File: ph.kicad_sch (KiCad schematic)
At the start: 38 parts, among them IC2 ADM3260ARSZ-RL7, J4 pH, U10 REF3020, U11 TPS60400DBV, U12 ADS1115IDGS, U14 TLV271, U15 TLV271

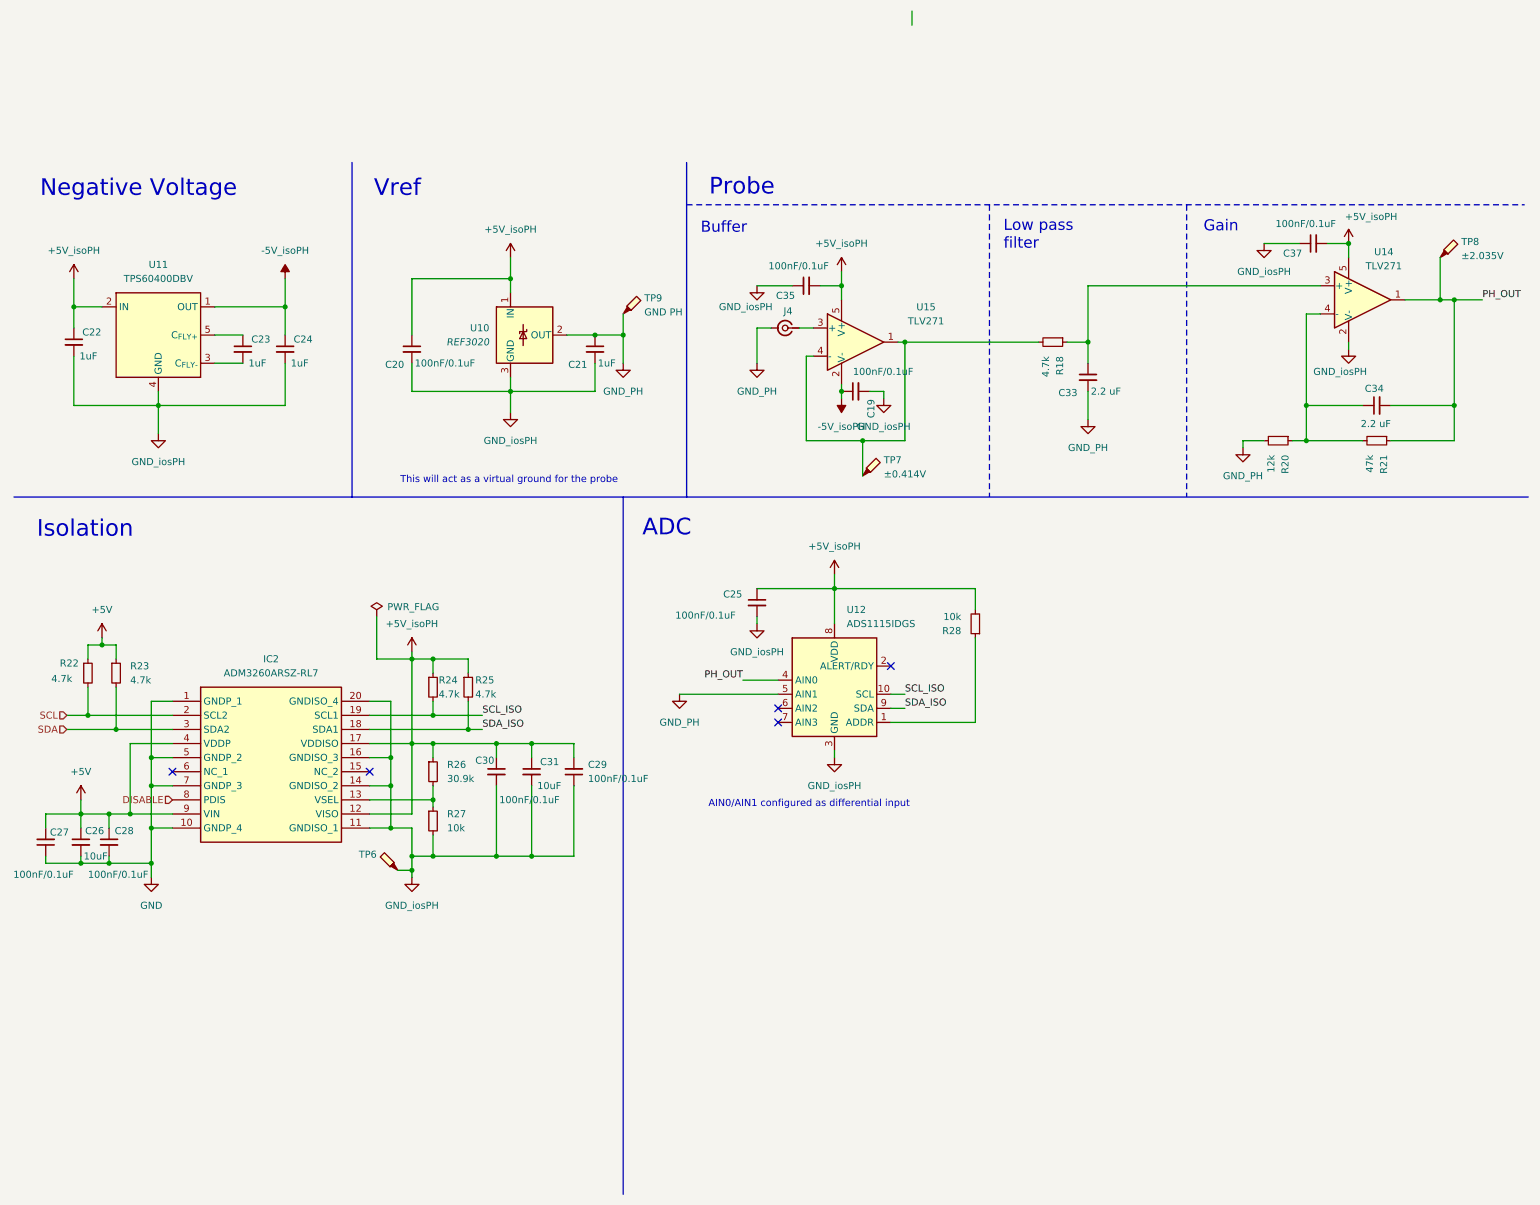
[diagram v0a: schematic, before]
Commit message: Fix ERC warnings
See #28
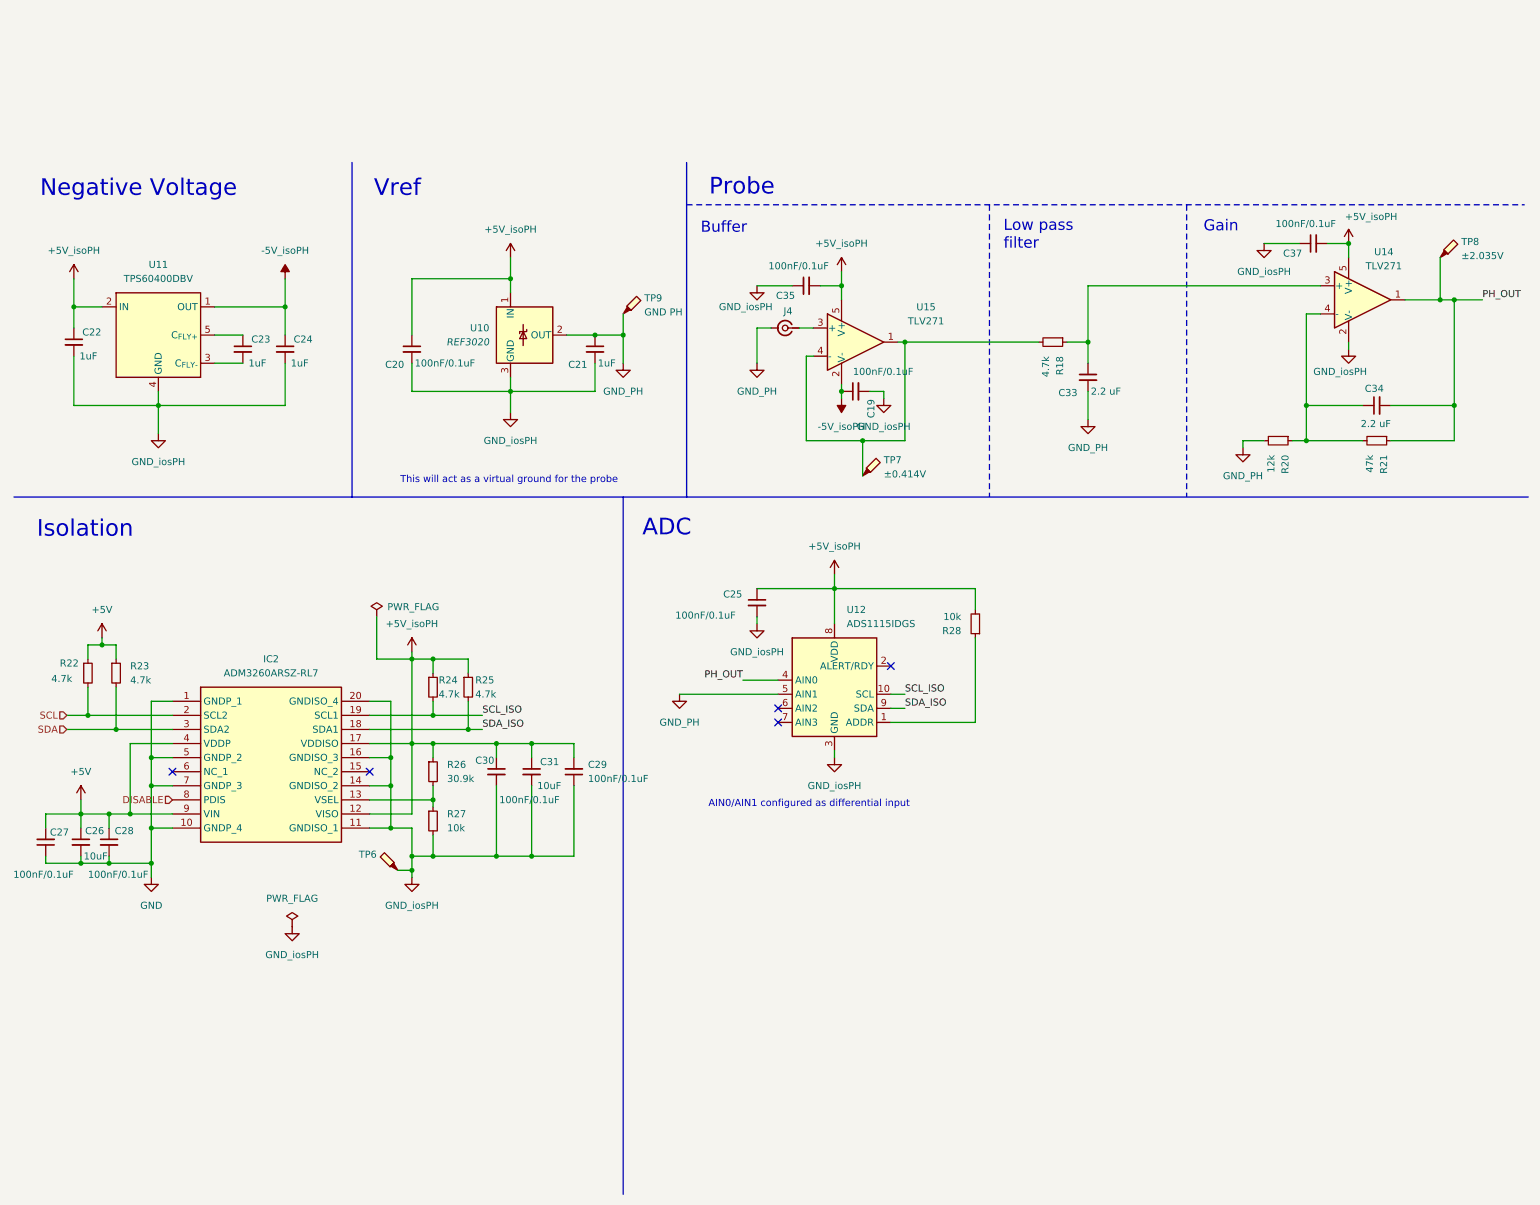
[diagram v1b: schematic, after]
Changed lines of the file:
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@@
 	(wire
 		(pts
-			(xy 173.99 -12.7) (xy 173.99 -15.24)
-		)
-		(stroke
-			(width 0)
-			(type default)
-		)
-	)
-	(wire
-		(pts
 			(xy 157.48 34.29) (xy 161.29 34.29)
 		)
@@
 	)
 	(symbol
+		(lib_id "power:GNDA")
+		(at 62.23 149.86 0)
+		(unit 1)
+		(exclude_from_sim no)
+		(in_bom yes)
+		(on_board yes)
+		(dnp no)
+		(fields_autoplaced yes)
+		(property "Reference" "#PWR0115"
+			(at 62.23 156.21 0)
+			(effects
+				(font
+					(size 1.27 1.27)
+				)
+				(hide yes)
+			)
+		)
+		(property "Value" "GND_iosPH"
+			(at 62.23 154.94 0)
+			(effects
+				(font
+					(size 1.27 1.27)
+				)
+			)
+		)
+		(property "Footprint" ""
+			(at 62.23 149.86 0)
+			(effects
+				(font
+					(size 1.27 1.27)
+				)
+				(hide yes)
+			)
+		)
+		(property "Datasheet" ""
+			(at 62.23 149.86 0)
+			(effects
+				(font
+					(size 1.27 1.27)
+				)
+				(hide yes)
+			)
+		)
+		(property "Description" "Power symbol creates a global label with name \"GNDA\" , analog ground"
+			(at 62.23 149.86 0)
+			(effects
+				(font
+					(size 1.27 1.27)
+				)
+				(hide yes)
+			)
+		)
+		(pin "1"
+		)
+		(instances
+			(project "HydroponicFlowerControl"
+				(path "/b3c8a28b-9ce1-4002-b8e8-ef8cb73fe031/98c7b1ae-5b10-4cce-8f75-2d85473487c0"
+					(reference "#PWR0115")
+					(unit 1)
+				)
+			)
+		)
+	)
+	(symbol
 		(lib_id "Connector:Conn_Coaxial_Small")
 		(at 151.13 41.91 180)
@@
 					(unit 1)
 				)
+			)
+		)
+	)
+	(symbol
+		(lib_id "power:PWR_FLAG")
+		(at 62.23 149.86 0)
+		(unit 1)
+		(exclude_from_sim no)
+		(in_bom yes)
+		(on_board yes)
+		(dnp no)
+		(fields_autoplaced yes)
+		(property "Reference" "#FLG08"
+			(at 62.23 147.955 0)
+			(effects
+				(font
+					(size 1.27 1.27)
+				)
+				(hide yes)
+			)
+		)
+		(property "Value" "PWR_FLAG"
+			(at 62.23 144.78 0)
+			(effects
+				(font
+					(size 1.27 1.27)
+				)
+			)
+		)
+		(property "Footprint" ""
+			(at 62.23 149.86 0)
+			(effects
+				(font
+					(size 1.27 1.27)
+				)
+				(hide yes)
+			)
+		)
+		(property "Datasheet" "~"
+			(at 62.23 149.86 0)
+			(effects
+				(font
+					(size 1.27 1.27)
+				)
+				(hide yes)
+			)
+		)
+		(property "Description" "Special symbol for telling ERC where power comes from"
+			(at 62.23 149.86 0)
+			(effects
+				(font
+					(size 1.27 1.27)
+				)
+				(hide yes)
+			)
+		)
+		(pin "1"
+		)
+		(instances
+			(project "HydroponicFlowerControl"
+				(path "/b3c8a28b-9ce1-4002-b8e8-ef8cb73fe031/98c7b1ae-5b10-4cce-8f75-2d85473487c0"
+					(reference "#FLG08")
+					(unit 1)
+				)

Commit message: Remove TPS60400 (U11) from pH block
Closes #30
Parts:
- removed C19: 100nF/0.1uF, Capacitor_SMD:C_0603_1608Metric, symbol Device:C_Small
- removed C22, C23, C24: 1uF, Capacitor_SMD:C_0603_1608Metric, symbol Device:C_Small
- removed U11: TPS60400DBV, Package_TO_SOT_SMD:SOT-23-5, symbol Regulator_SwitchedCapacitor:TPS60400DBV
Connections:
- net -5V_isoPH is gone; now on net GND_iosPH: U15.2 (V-)
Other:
- note removed: "Negative Voltage"

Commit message: Update pH connector to combined BNC and SMA footprint
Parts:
- J4: footprint Connector_Coaxial:BNC_Amphenol_B6252HB-NPP3G-50_Horizontal -> HydroponicFlowerControl:BNC_SMA; LCSC C2837587 -> (none); LCSC bnc (none) -> C2837587; LCSC sma (none) -> C496550
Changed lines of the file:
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@@
 			)
 		)
-		(property "Footprint" "Connector_Coaxial:BNC_Amphenol_B6252HB-NPP3G-50_Horizontal"
+		(property "Footprint" "HydroponicFlowerControl:BNC_SMA"
 			(at 151.13 41.91 0)
 			(effects
@@
 			)
 		)
-		(property "LCSC" "C2837587"
+		(property "LCSC bnc" "C2837587"
 			(at 151.13 41.91 0)
 			(effects
+				(font
+					(size 1.27 1.27)
+				)
+				(hide yes)
+			)
+		)
+		(property "LCSC sma" "C496550"
+			(at 151.13 41.91 0)
+			(effects

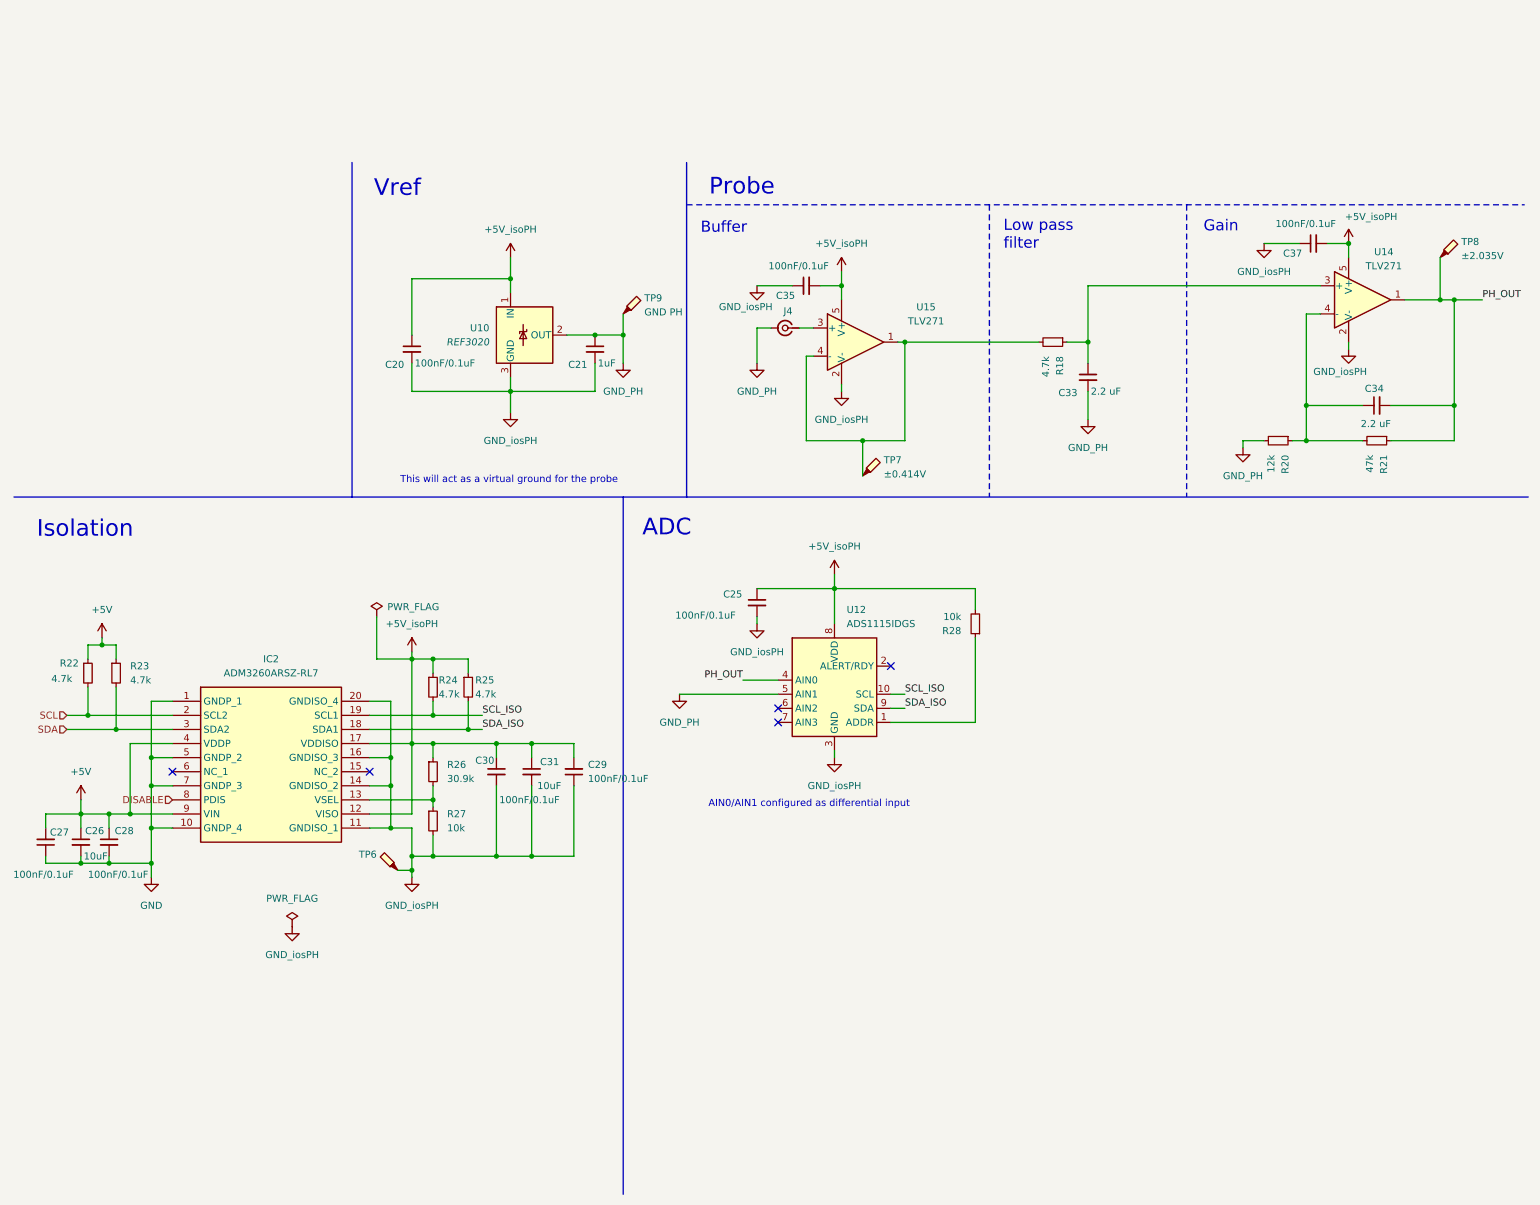
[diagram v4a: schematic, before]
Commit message: Remove pH circuits
And replace with a header to connect to an external HAT board
Closes #40
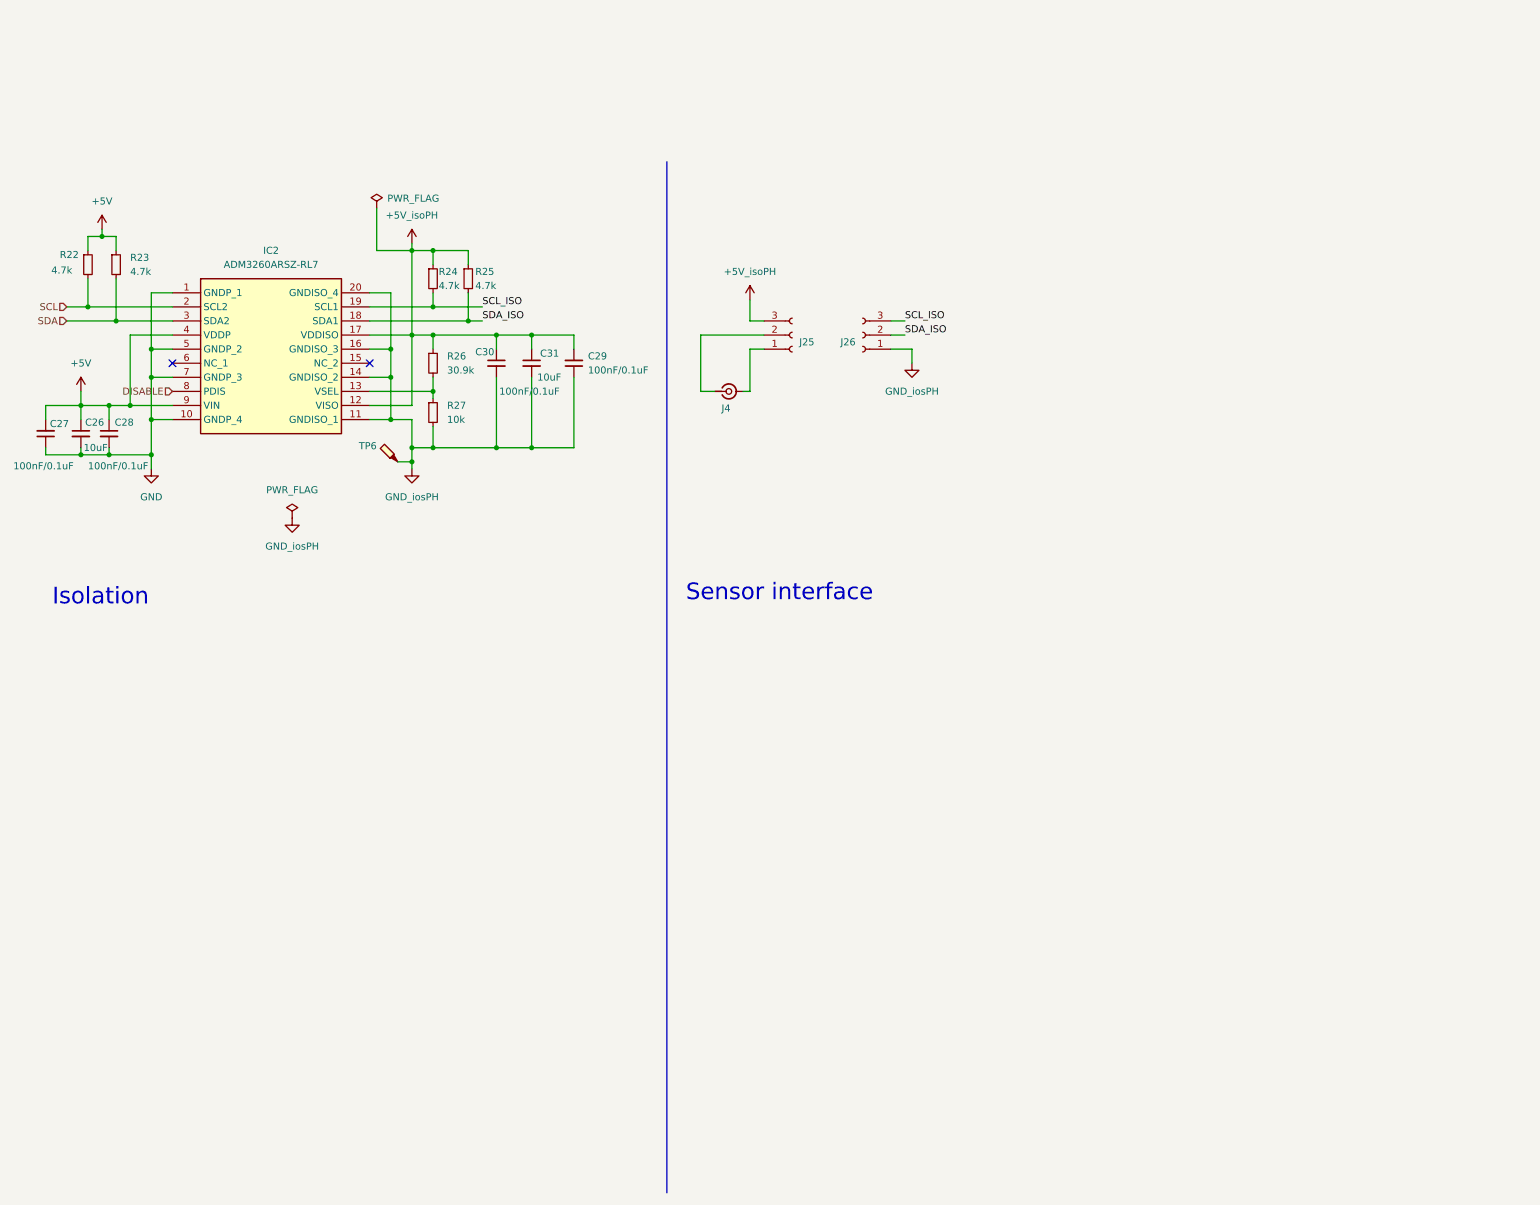
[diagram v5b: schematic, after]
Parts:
- removed C20, C25, C35, C37: 100nF/0.1uF, Capacitor_SMD:C_0603_1608Metric, symbol Device:C_Small
- removed C21: 1uF, Capacitor_SMD:C_0603_1608Metric, symbol Device:C_Small
- removed C33, C34: 2.2 uF, Capacitor_SMD:C_0603_1608Metric, symbol Device:C_Small
- removed R18: 4.7k, Resistor_SMD:R_0603_1608Metric, symbol Device:R_Small
- removed R20: 12k, Resistor_SMD:R_0603_1608Metric, symbol Device:R_Small
- removed R21: 47k, Resistor_SMD:R_0603_1608Metric, symbol Device:R_Small
- removed R28: 10k, Resistor_SMD:R_0603_1608Metric, symbol Device:R_Small
- removed TP7: ±0.414V, TestPoint:TestPoint_Pad_D1.0mm, symbol Connector:TestPoint_Probe
- removed TP8: ±2.035V, TestPoint:TestPoint_Pad_D1.0mm, symbol Connector:TestPoint_Probe
- removed TP9: GND PH, TestPoint:TestPoint_Pad_D1.0mm, symbol Connector:TestPoint_Probe
- removed U10: REF3020, Package_TO_SOT_SMD:SOT-23, symbol Reference_Voltage:REF3020
- removed U12: ADS1115IDGS, Package_SO:VSSOP-10_3x3mm_P0.5mm, symbol Analog_ADC:ADS1115IDGS
- removed U14, U15: TLV271, Package_TO_SOT_SMD:SOT-23-5, symbol Amplifier_Operational:TLV2371DBV
- added J25, J26: Conn_01x03_Socket, Connector_PinSocket_2.54mm:PinSocket_1x03_P2.54mm_Vertical, symbol Connector:Conn_01x03_Socket
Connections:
- net +5V_isoPH: now also J25.3 (Pin_3)
- net GND_iosPH: now also J26.1 (Pin_1)
- net SCL_ISO: now also J26.3 (Pin_3)
- net SDA_ISO: now also J26.2 (Pin_2)
- net at J4.1 (In): now also J25.2 (Pin_2)
- net GND_PH: no longer names the net of J4.2 (Ext)
- net GND_PH: now also J25.1 (Pin_1)
- no-connect marks 5 -> 2
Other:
- note added: "Sensor interface"
- note removed: "ADC"
- note removed: "AIN0/AIN1 configured as differential input"
- note removed: "Buffer"
- note removed: "Gain"
- note removed: "Low pass filter"
- note removed: "Probe"
- note removed: "This will act as a virtual ground for the probe"
- note removed: "Vref"
- moved on the sheet: C26, C27, C28, C29, C30, C31, IC2, J4, R22, R23, R24, R25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

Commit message: Update manufacturing positions and rotations of parts
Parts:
- J25, J26: JLCPCB Rotation Offset (none) -> 90
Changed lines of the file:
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@@
+			)
+		)
+		(property "JLCPCB Rotation Offset" "90"
+			(at 165.1 43.18 0)
+			(effects
+				(font
+					(size 1.27 1.27)
+				)
+				(hide yes)
 			)
 		)
@@
 			(at 152.4 43.18 0)
 			(effects
+				(font
+					(size 1.27 1.27)
+				)
+				(hide yes)
+			)
+		)
+		(property "JLCPCB Rotation Offset" "90"
+			(at 152.4 43.18 0)
+			(effects

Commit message: Include THT components in manufacturing
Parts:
- J25, J26: now in the parts list
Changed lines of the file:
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@@
 		(unit 1)
 		(exclude_from_sim no)
-		(in_bom no)
+		(in_bom yes)
 		(on_board yes)
 		(dnp no)
@@
 		(unit 1)
 		(exclude_from_sim no)
-		(in_bom no)
-		(on_board yes)
-		(dnp no)
+		(in_bom yes)
+		(on_board yes)
+		(dnp no)
